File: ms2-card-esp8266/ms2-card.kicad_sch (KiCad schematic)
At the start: 63 parts, among them J1 Schaltregler, J10 MicroSD_SPI_CD, J11 Conn_01x06, J2 ESP Prog, J20 Smartcard Connector, J21 PogoPin, J22 Card Edge, J23 Conn_01x04, J30 USB_B_Micro, J31 Power Select, J32 Conn_01x03, Q1 MMBT3904, Q2 MMBT3904, Q3 MMBT5401, SW1 RESET, U1 ESP-12F, U10 W25Q128JVIM, U2 FM24C64B, U20 BL1551B, U3 BL1551B, U30 CP2102N-A02-GQFN24R, U4 BL1551B, U6 AMS1117-3.3

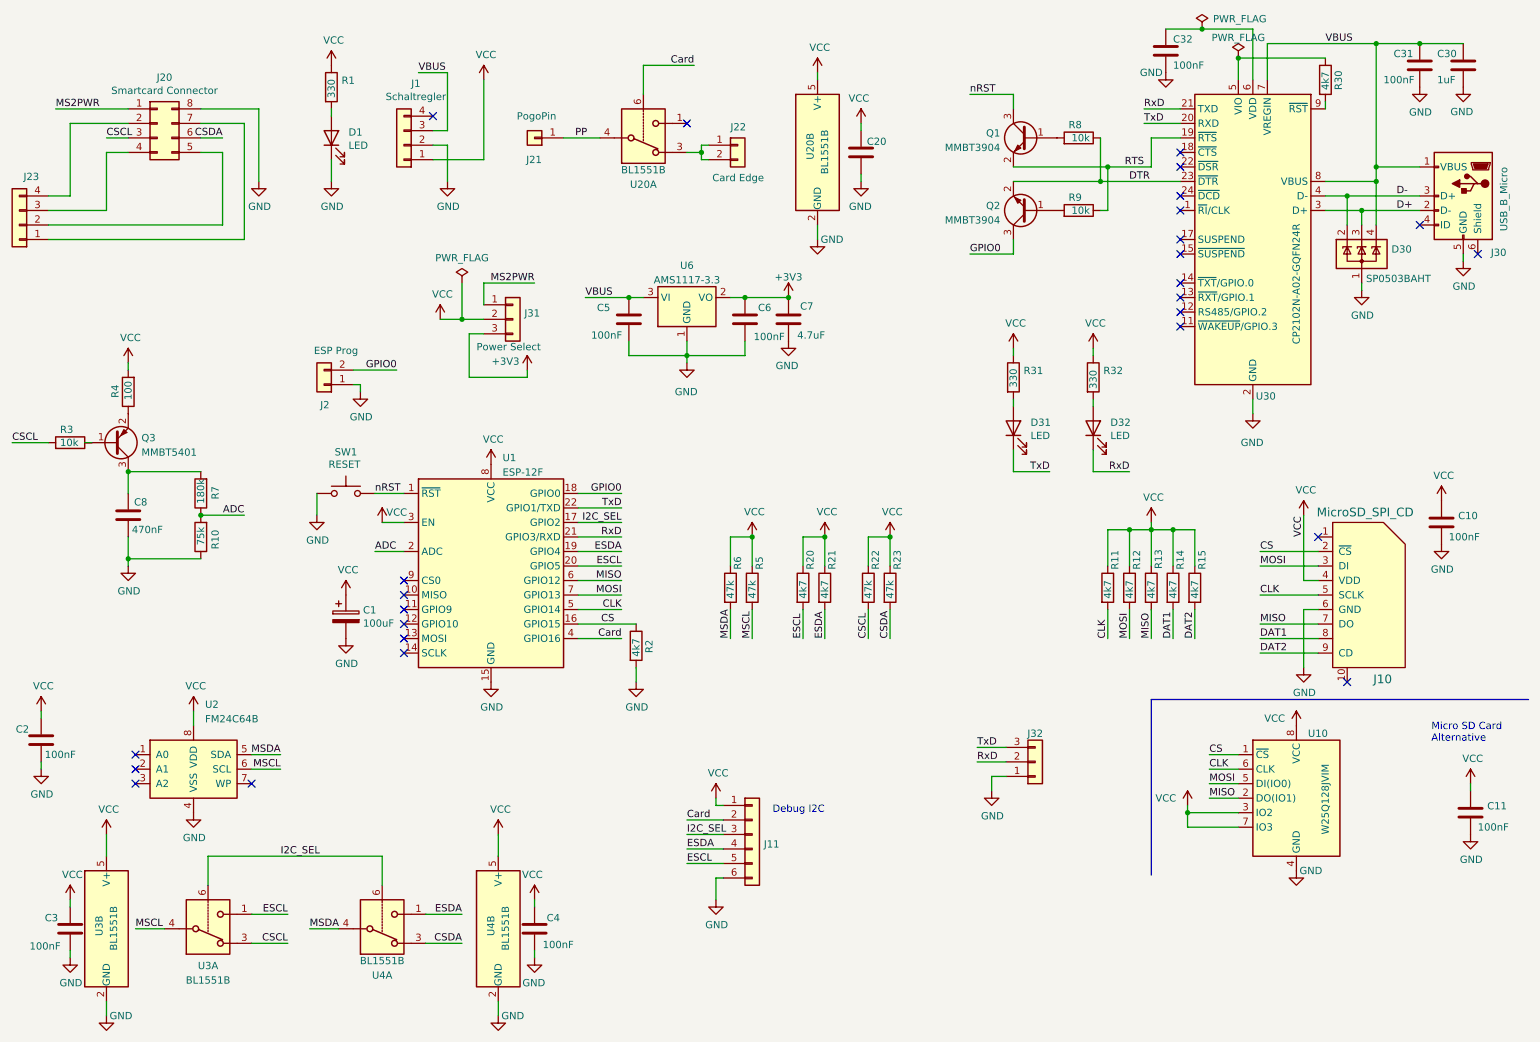
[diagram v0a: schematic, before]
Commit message: elimate errors sourced by KiCad update
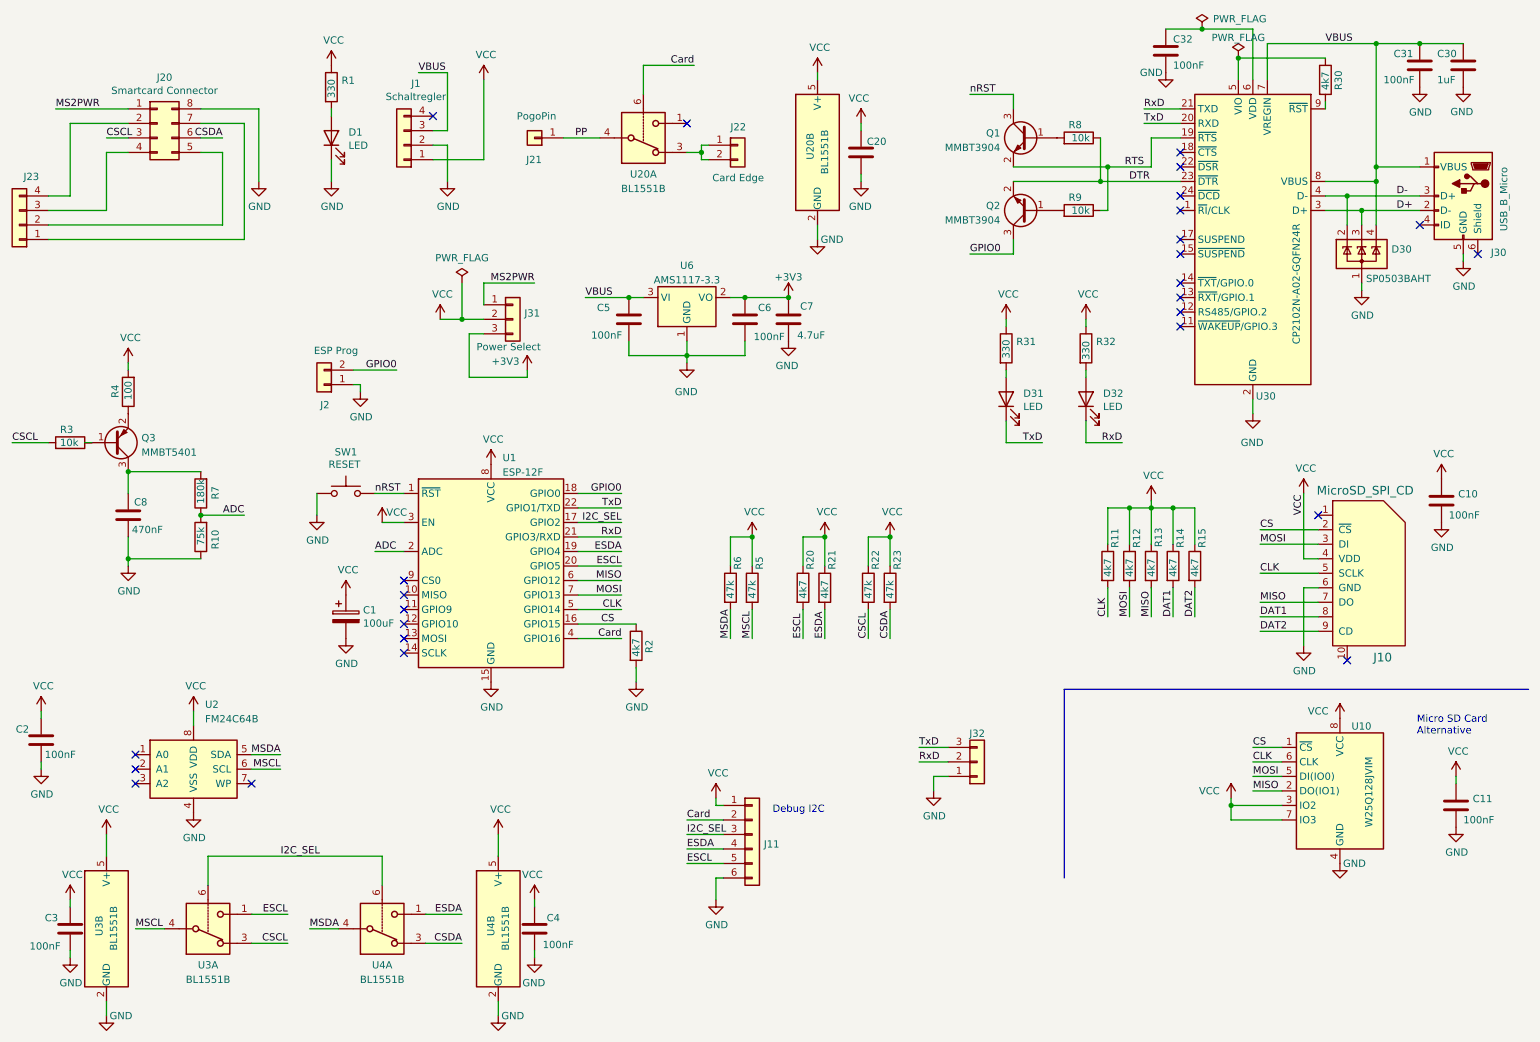
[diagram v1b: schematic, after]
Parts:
- J20: footprint w_conn_misc:iso7816_conn -> MS2-Card:iso7816_conn
- U1: JLCPCB Position Offset 4.03,0.0 -> 0,0,0.0
- U10: footprint Package_SO:SOIC-8_5.23x5.23mm_P1.27mm -> Package_SO:SOIC-8_3.9x4.9mm_P1.27mm
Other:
- moved on the sheet: C10, C11, D31, D32, J10, J32, R11, R12, R13, R14, R15, R31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

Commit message: fix rotation / most are done by JLCPCB Fabrication Plugin
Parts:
- D30: JLCPCB Rotation Offset -90 -> 90
- J10: JLCPCB Position Offset 5.73,0.0 -> 0.0,0.0
- Q1, Q2, Q3, U20, U3, U4, U6: JLCPCB Rotation Offset 180 -> (none)
- U2: JLCPCB Rotation Offset -90 -> (none)
- U30: JLCPCB Rotation Offset (none) -> -90
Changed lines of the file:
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@@
-      (effects (font (size 1.27 1.27)) hide)
-    )
-    (property "JLCPCB Rotation Offset" "-90" (at 49.53 146.05 0)
       (effects (font (size 1.27 1.27)) hide)
     )
@@
       (effects (font (size 1.27 1.27)) hide)
     )
-    (property "JLCPCB Rotation Offset" "180" (at 102.87 173.99 0)
-      (effects (font (size 1.27 1.27)) hide)
-    )
     (pin "1")
     (pin "3")
@@
     )
     (property "LCSC" "C2944066" (at 34.29 173.99 0)
-      (effects (font (size 1.27 1.27)) hide)
-    )
-    (property "JLCPCB Rotation Offset" "180" (at 34.29 173.99 0)
       (effects (font (size 1.27 1.27)) hide)
     )
@@
     )
     (property "LCSC" "C969151" (at 234.95 53.34 0)
+      (effects (font (size 1.27 1.27)) hide)
+    )
+    (property "JLCPCB Rotation Offset" "-90" (at 234.95 53.34 0)
       (effects (font (size 1.27 1.27)) hide)
     )
@@
       (effects (font (size 1.27 1.27)) hide)
     )
-    (property "JLCPCB Rotation Offset" "180" (at 52.07 173.99 0)
-      (effects (font (size 1.27 1.27)) hide)
-    )
     (pin "1")
     (pin "3")
@@
       (effects (font (size 1.27 1.27)) hide)
     )
-    (property "JLCPCB Rotation Offset" "-90" (at 254 55.88 0)
+    (property "JLCPCB Rotation Offset" "90" (at 254 55.88 0)
       (effects (font (size 1.27 1.27)) hide)
     )
@@
     )
     (property "LCSC" "C2944066" (at 128.27 35.56 0)
-      (effects (font (size 1.27 1.27)) hide)
-    )
-    (property "JLCPCB Rotation Offset" "180" (at 128.27 35.56 0)
       (effects (font (size 1.27 1.27)) hide)
     )
@@
       (effects (font (size 1.27 1.27)) hide)
     )
-    (property "JLCPCB Rotation Offset" "180" (at 35.56 88.9 0)
-      (effects (font (size 1.27 1.27)) hide)
-    )
     (pin "1")
     (pin "2")
@@
     )
     (property "LCSC" "C20526" (at 195.58 35.56 0)
-      (effects (font (size 1.27 1.27)) hide)
-    )
-    (property "JLCPCB Rotation Offset" "180" (at 195.58 35.56 0)
       (effects (font (size 1.27 1.27)) hide)
     )
@@
       (effects (font (size 1.27 1.27)) hide)
     )
-    (property "JLCPCB Rotation Offset" "180" (at 158.75 38.1 0)
-      (effects (font (size 1.27 1.27)) hide)
-    )
     (pin "1")
     (pin "3")
@@
       (effects (font (size 1.27 1.27)) hide)
     )
-    (property "JLCPCB Rotation Offset" "180" (at 135.89 63.5 0)
-      (effects (font (size 1.27 1.27)) hide)
-    )
     (pin "1")
     (pin "2")
@@
     )
     (property "LCSC" "C2944066" (at 82.55 173.99 0)
-      (effects (font (size 1.27 1.27)) hide)
-    )
-    (property "JLCPCB Rotation Offset" "180" (at 82.55 173.99 0)
       (effects (font (size 1.27 1.27)) hide)
     )
@@
       (effects (font (size 1.27 1.27)) hide)
     )
-    (property "JLCPCB Position Offset" "5.73,0.0" (at 255.27 111.76 0)
+    (property "JLCPCB Position Offset" "0.0,0.0" (at 255.27 111.76 0)
       (effects (font (size 1.27 1.27)) hide)
     )
@@
       (effects (font (size 1.27 1.27)) hide)
     )
-    (property "JLCPCB Rotation Offset" "180" (at 195.58 48.26 0)
-      (effects (font (size 1.27 1.27)) hide)
-    )

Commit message: fix error messages
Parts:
- removed U10: W25Q128JVIM, Package_SO:SOIC-8_3.9x4.9mm_P1.27mm, symbol Memory_Flash:W25Q32JVSS
- added U10: W25Q128JM, Package_SO:SOIC-8_3.9x4.9mm_P1.27mm, symbol Memory_EEPROM:25LCxxx
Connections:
- net CLK: now also U10.6 (SCK)
- net CS: now also U10.1 (~{CS})
- net GND: now also U10.4 (GND)
- net MISO: now also U10.2 (MISO)
- net MOSI: now also U10.5 (MOSI)
- net VCC: now also U10.3 (~{WP}), U10.7 (~{HOLD}), U10.8 (VCC)
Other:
- moved on the sheet: C11

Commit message: fix production offset
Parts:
- J10: JLCPCB Position Offset 0.0,0.0 -> 0.0,5.73
- U1: JLCPCB Position Offset 0,0,0.0 -> 0.0,-4.03
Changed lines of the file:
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@@
       (effects (font (size 1.27 1.27)) hide)
     )
-    (property "JLCPCB Position Offset" "0,0,0.0" (at 101.6 113.03 0)
+    (property "JLCPCB Position Offset" "0.0,-4.03" (at 101.6 113.03 0)
       (effects (font (size 1.27 1.27)) hide)
     )
@@
       (effects (font (size 1.27 1.27)) hide)
     )
-    (property "JLCPCB Position Offset" "0.0,0.0" (at 255.27 111.76 0)
-      (effects (font (size 1.27 1.27)) hide)
-    )
+    (property "JLCPCB Position Offset" "0.0,5.73" (at 255.27 111.76 0)
+      (effects (font (size 1.27 1.27)) hide)
+    )

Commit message: fix ESP-12F offset
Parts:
- U1: JLCPCB Position Offset 0.0,-4.03 -> 0.0,-4.13
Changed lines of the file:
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@@
       (effects (font (size 1.27 1.27)) hide)
     )
-    (property "JLCPCB Position Offset" "0.0,-4.03" (at 101.6 113.03 0)
+    (property "JLCPCB Position Offset" "0.0,-4.13" (at 101.6 113.03 0)
       (effects (font (size 1.27 1.27)) hide)
     )

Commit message: use modified PogoPin footprint for easier production
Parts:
- J21: footprint PogoPin:PogoPin -> PogoPin:PogoPin2
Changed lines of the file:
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@@
       (effects (font (size 1.27 1.27)) (justify left))
     )
-    (property "Footprint" "PogoPin:PogoPin" (at 109.22 35.56 0)
+    (property "Footprint" "PogoPin:PogoPin2" (at 109.22 35.56 0)
       (effects (font (size 1.27 1.27)) hide)
     )

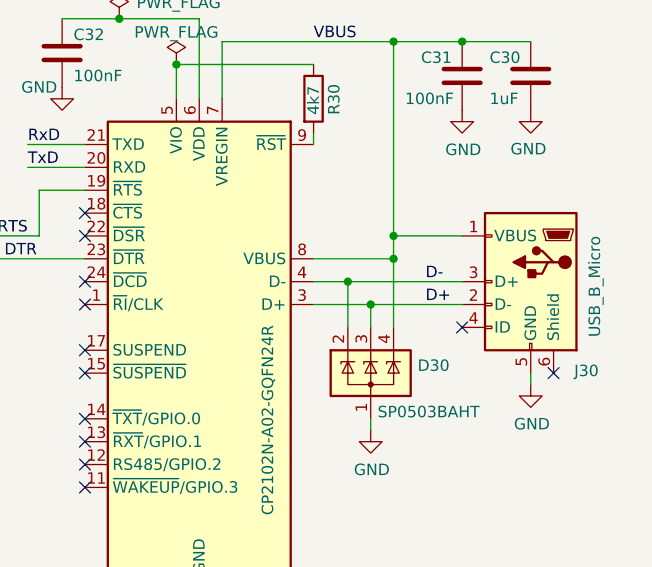
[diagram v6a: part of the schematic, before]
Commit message: fix USB D+/D- swap
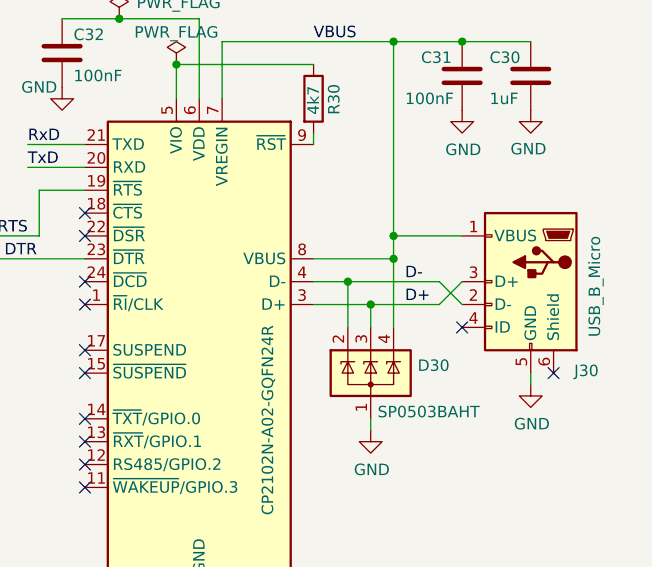
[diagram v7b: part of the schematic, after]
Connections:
- net D+: now also J30.3 (D+); no longer J30.2 (D-)
- net D-: now also J30.2 (D-); no longer J30.3 (D+)
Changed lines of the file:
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@@
   (junction (at 256.54 40.64) (diameter 0) (color 0 0 0 0)
   )
+  (junction (at 218.44 147.32) (diameter 0) (color 0 0 0 0)
+  )
+  (junction (at 208.28 43.18) (diameter 0) (color 0 0 0 0)
+  )
+  (junction (at 226.06 16.51) (diameter 0) (color 0 0 0 0)
+  )
+  (junction (at 264.16 19.05) (diameter 0) (color 0 0 0 0)
+  )
+  (junction (at 135.89 73.66) (diameter 0) (color 0 0 0 0)
+  )
+  (junction (at 220.98 100.33) (diameter 0) (color 0 0 0 0)
+  )
+  (junction (at 171.45 105.41) (diameter 0) (color 0 0 0 0)
+  )
+  (junction (at 209.55 40.64) (diameter 0) (color 0 0 0 0)
+  )
+  (junction (at 153.67 63.5) (diameter 0) (color 0 0 0 0)
+  )
+  (junction (at 256.54 43.18) (diameter 0) (color 0 0 0 0)
+  )
+  (junction (at 160.02 105.41) (diameter 0) (color 0 0 0 0)
+  )
+  (junction (at 38.1 93.98) (diameter 0) (color 0 0 0 0)
+  )
+  (junction (at 146.05 63.5) (diameter 0) (color 0 0 0 0)
+  )
+  (junction (at 217.17 100.33) (diameter 0) (color 0 0 0 0)
+  )
+  (junction (at 50.8 101.6) (diameter 0) (color 0 0 0 0)
+  )
+  (junction (at 147.32 105.41) (diameter 0) (color 0 0 0 0)
+  )
+  (junction (at 254 48.26) (diameter 0) (color 0 0 0 0)
+  )
   (junction (at 251.46 45.72) (diameter 0) (color 0 0 0 0)
   )
-  (junction (at 218.44 147.32) (diameter 0) (color 0 0 0 0)
-  )
-  (junction (at 208.28 43.18) (diameter 0) (color 0 0 0 0)
-  )
-  (junction (at 226.06 16.51) (diameter 0) (color 0 0 0 0)
-  )
-  (junction (at 264.16 19.05) (diameter 0) (color 0 0 0 0)
-  )
-  (junction (at 135.89 73.66) (diameter 0) (color 0 0 0 0)
-  )
-  (junction (at 220.98 100.33) (diameter 0) (color 0 0 0 0)
-  )
-  (junction (at 171.45 105.41) (diameter 0) (color 0 0 0 0)
-  )
-  (junction (at 209.55 40.64) (diameter 0) (color 0 0 0 0)
-  )
-  (junction (at 153.67 63.5) (diameter 0) (color 0 0 0 0)
-  )
-  (junction (at 256.54 43.18) (diameter 0) (color 0 0 0 0)
-  )
-  (junction (at 160.02 105.41) (diameter 0) (color 0 0 0 0)
-  )
-  (junction (at 38.1 93.98) (diameter 0) (color 0 0 0 0)
-  )
-  (junction (at 146.05 63.5) (diameter 0) (color 0 0 0 0)
-  )
-  (junction (at 217.17 100.33) (diameter 0) (color 0 0 0 0)
-  )
-  (junction (at 50.8 101.6) (diameter 0) (color 0 0 0 0)
-  )
-  (junction (at 147.32 105.41) (diameter 0) (color 0 0 0 0)
-  )
   (junction (at 125.73 63.5) (diameter 0) (color 0 0 0 0)
-  )
-  (junction (at 254 48.26) (diameter 0) (color 0 0 0 0)
   )
   (no_connect (at 222.25 60.96))
@@
     (stroke (width 0) (type default))
   )
+  (wire (pts (xy 261.62 48.26) (xy 254 48.26))
+    (stroke (width 0) (type default))
+  )
   (wire (pts (xy 116.84 105.41) (xy 124.46 105.41))
     (stroke (width 0) (type default))
@@
     (stroke (width 0) (type default))
   )
-  (wire (pts (xy 254 48.26) (xy 264.16 48.26))
-    (stroke (width 0) (type default))
-  )
   (wire (pts (xy 27.94 177.8) (xy 27.94 179.07))
     (stroke (width 0) (type default))
@@
     (stroke (width 0) (type default))
   )
+  (wire (pts (xy 264.16 48.26) (xy 261.62 45.72))
+    (stroke (width 0) (type default))
+  )
   (wire (pts (xy 218.44 149.86) (xy 218.44 147.32))
     (stroke (width 0) (type default))
@@
     (stroke (width 0) (type default))
   )
+  (wire (pts (xy 264.16 45.72) (xy 261.62 48.26))
+    (stroke (width 0) (type default))
+  )
   (wire (pts (xy 241.3 152.4) (xy 246.38 152.4))
     (stroke (width 0) (type default))
@@
     (stroke (width 0) (type default))
   )
+  (wire (pts (xy 261.62 45.72) (xy 251.46 45.72))
+    (stroke (width 0) (type default))
+  )
   (wire (pts (xy 247.65 29.21) (xy 247.65 30.48))
     (stroke (width 0) (type default))
@@
     (stroke (width 0) (type default))
   )
-  (wire (pts (xy 251.46 45.72) (xy 264.16 45.72))
-    (stroke (width 0) (type default))
-  )
   (wire (pts (xy 146.05 71.12) (xy 146.05 73.66))
     (stroke (width 0) (type default))
@@
     (effects (font (size 1.27 1.27)) (justify left bottom))
   )
-  (label "D-" (at 260.096 45.72 0) (fields_autoplaced)
+  (label "D-" (at 257.81 45.72 0) (fields_autoplaced)
     (effects (font (size 1.27 1.27)) (justify left bottom))
   )
@@
     (effects (font (size 1.27 1.27)) (justify left bottom))
   )
-  (label "D+" (at 260.096 48.26 0) (fields_autoplaced)
-    (effects (font (size 1.27 1.27)) (justify left bottom))
-  )
+  (label "D+" (at 257.81 48.26 0) (fields_autoplaced)
+    (effects (font (size 1.27 1.27)) (justify left bottom))
+  )

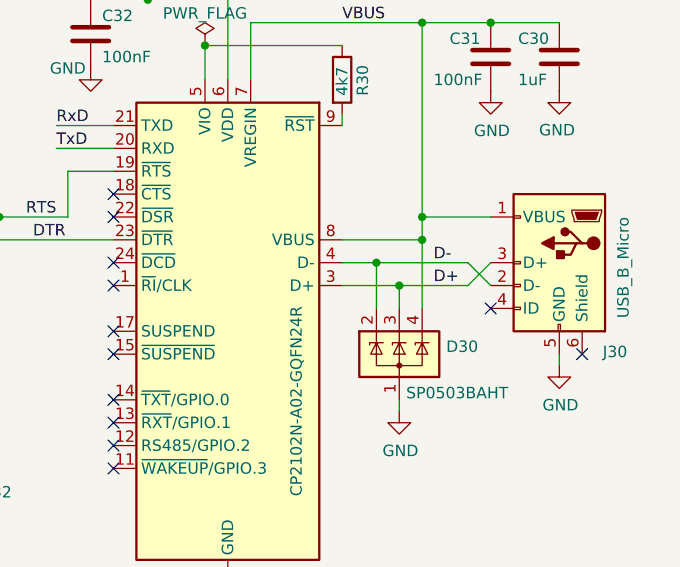
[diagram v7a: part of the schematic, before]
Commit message: fix USB D+/D- swap
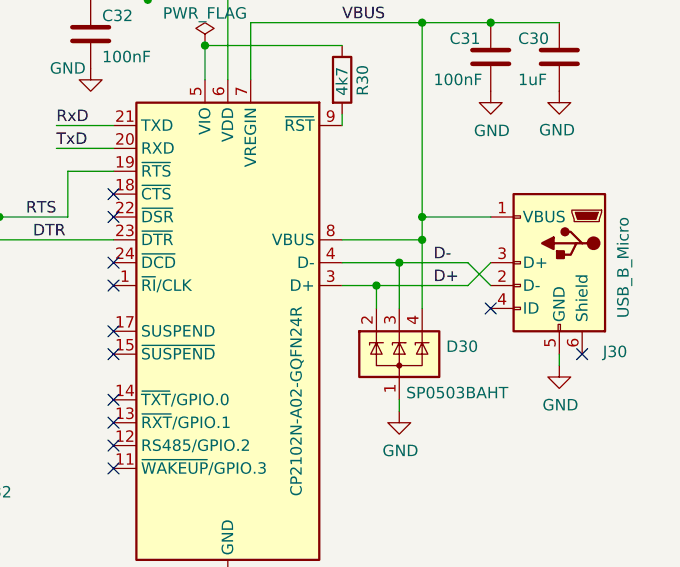
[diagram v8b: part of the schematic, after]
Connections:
- net D+: now also D30.2 (K); no longer D30.3 (K)
- net D-: now also D30.3 (K); no longer D30.2 (K)
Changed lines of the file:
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@@
     (comment 1 "Gerhard Bertelsmann")
   )
+  (junction (at 251.46 48.26) (diameter 0) (color 0 0 0 0)
+  )
   (junction (at 232.41 21.59) (diameter 0) (color 0 0 0 0)
   )
@@
   (junction (at 153.67 63.5) (diameter 0) (color 0 0 0 0)
   )
+  (junction (at 254 45.72) (diameter 0) (color 0 0 0 0)
+  )
   (junction (at 256.54 43.18) (diameter 0) (color 0 0 0 0)
   )
@@
   )
   (junction (at 147.32 105.41) (diameter 0) (color 0 0 0 0)
-  )
-  (junction (at 254 48.26) (diameter 0) (color 0 0 0 0)
-  )
-  (junction (at 251.46 45.72) (diameter 0) (color 0 0 0 0)
   )
   (junction (at 125.73 63.5) (diameter 0) (color 0 0 0 0)
@@
     (stroke (width 0) (type default))
   )
+  (wire (pts (xy 251.46 48.26) (xy 261.62 48.26))
+    (stroke (width 0) (type default))
+  )
   (wire (pts (xy 160.02 118.11) (xy 160.02 123.19))
     (stroke (width 0) (type default))
@@
     (stroke (width 0) (type default))
   )
+  (wire (pts (xy 254 45.72) (xy 261.62 45.72))
+    (stroke (width 0) (type default))
+  )
   (wire (pts (xy 109.22 177.8) (xy 109.22 179.07))
     (stroke (width 0) (type default))
@@
     (stroke (width 0) (type default))
   )
-  (wire (pts (xy 261.62 48.26) (xy 254 48.26))
-    (stroke (width 0) (type default))
-  )
   (wire (pts (xy 116.84 105.41) (xy 124.46 105.41))
     (stroke (width 0) (type default))
@@
     (stroke (width 0) (type default))
   )
+  (wire (pts (xy 254 50.8) (xy 254 45.72))
+    (stroke (width 0) (type default))
+  )
   (wire (pts (xy 140.97 151.13) (xy 140.97 152.4))
     (stroke (width 0) (type default))
@@
     (stroke (width 0) (type default))
   )
-  (wire (pts (xy 247.65 45.72) (xy 251.46 45.72))
+  (wire (pts (xy 247.65 45.72) (xy 254 45.72))
     (stroke (width 0) (type default))
   )
@@
     (stroke (width 0) (type default))
   )
+  (wire (pts (xy 251.46 50.8) (xy 251.46 48.26))
+    (stroke (width 0) (type default))
+  )
   (wire (pts (xy 241.3 149.86) (xy 246.38 149.86))
     (stroke (width 0) (type default))
@@
     (stroke (width 0) (type default))
   )
-  (wire (pts (xy 261.62 45.72) (xy 251.46 45.72))
-    (stroke (width 0) (type default))
-  )
   (wire (pts (xy 247.65 29.21) (xy 247.65 30.48))
     (stroke (width 0) (type default))
@@
     (stroke (width 0) (type default))
   )
-  (wire (pts (xy 254 48.26) (xy 254 50.8))
-    (stroke (width 0) (type default))
-  )
-  (wire (pts (xy 247.65 48.26) (xy 254 48.26))
+  (wire (pts (xy 247.65 48.26) (xy 251.46 48.26))
     (stroke (width 0) (type default))
   )
@@
     (stroke (width 0) (type default))
   )
-  (wire (pts (xy 251.46 45.72) (xy 251.46 50.8))
-    (stroke (width 0) (type default))
-  )
